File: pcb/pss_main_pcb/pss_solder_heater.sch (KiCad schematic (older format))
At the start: 43 parts, among them J3 Hot Air Gun, J4 Soldering Iron, Q1 BC817, Q2 MMBT2222, Q3 MMBT2907, Q4 IRLML9301T, Q5 IRFZ44S, Q6 BT139B-800, U3 MOC3023S, U4 LM358

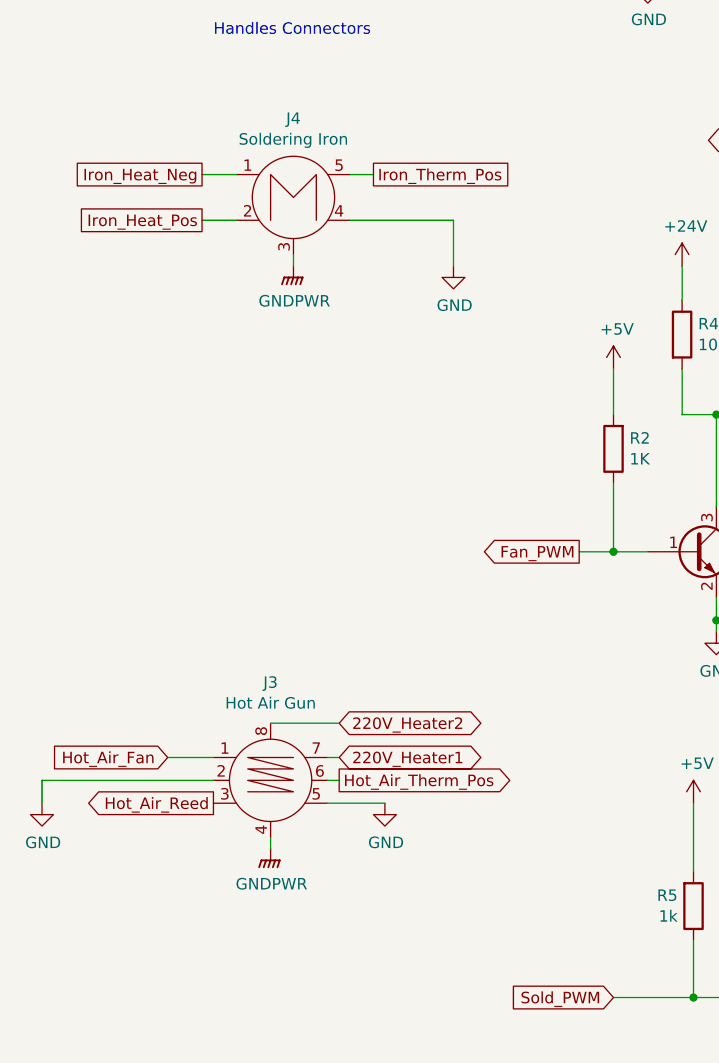
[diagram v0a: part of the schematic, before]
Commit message: Change footprints and place some new components
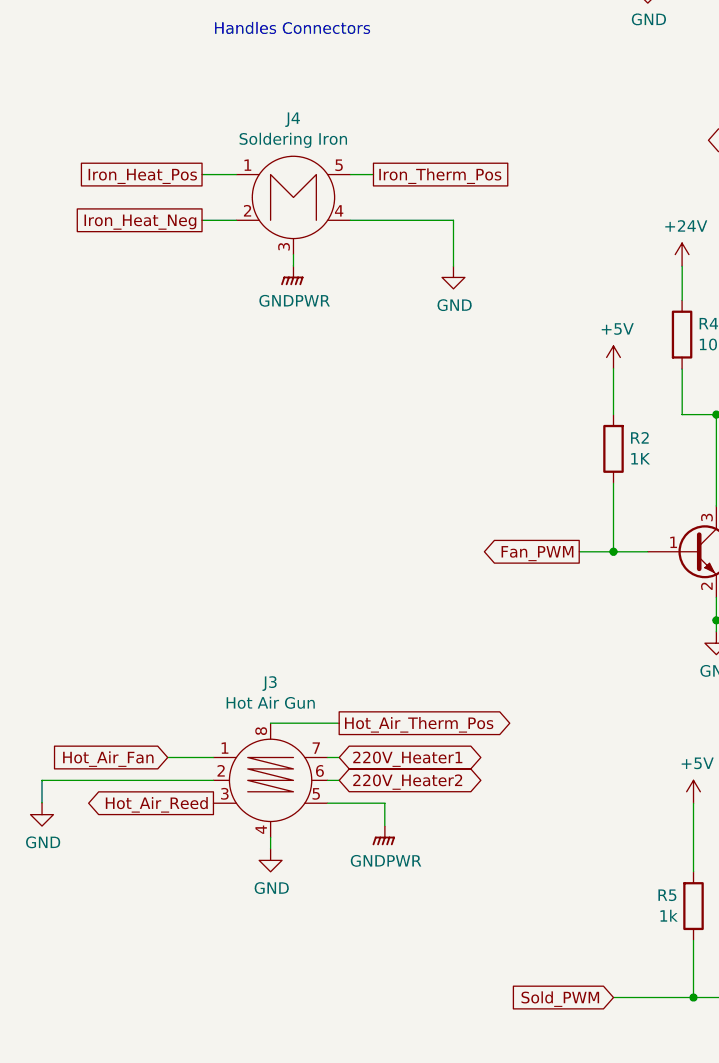
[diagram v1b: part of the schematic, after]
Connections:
- net +24V: now also J4.1; no longer J4.2
- net 220V_Heater2: now also J3.6; no longer J3.8
- net GND: now also J3.4; no longer J3.5
- net GNDPWR: now also J3.5; no longer J3.4
- net Hot_Air_Therm_Pos: now also J3.8; no longer J3.6
- net Iron_Heat_Neg: now also J4.2; no longer J4.1
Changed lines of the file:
@@
 L power:GNDPWR #PWR?
 U 1 1 5EB844F4
-P 1750 5700
+P 2250 5600
 AR Path="/5EB844F4" Ref="#PWR?"  Part="1"
 AR Path="/5EE027BC/5EB844F4" Ref="#PWR?"  Part="1"
 AR Path="/5EE1CBE0/5EB844F4" Ref="#PWR013"  Part="1"
-F 0 "#PWR013" H 1750 5500 50  0001 C CNN
-F 1 "GNDPWR" H 1754 5546 50  0000 C CNN
-F 2 "" H 1750 5650 50  0001 C CNN
-F 3 "" H 1750 5650 50  0001 C CNN
-	1    1750 5700
+F 0 "#PWR013" H 2250 5400 50  0001 C CNN
+F 1 "GNDPWR" H 2254 5446 50  0000 C CNN
+F 2 "" H 2250 5550 50  0001 C CNN
+F 3 "" H 2250 5550 50  0001 C CNN
+	1    2250 5600
 	1    0    0    -1
 $EndComp
 Wire Wire Line
 	1750 5700 1750 5650
-Text GLabel 1450 2950 0    50   UnSpc ~ 0
+Text GLabel 1450 2750 0    50   UnSpc ~ 0
 Iron_Heat_Pos
 Wire Wire Line
 	1450 2750 1600 2750
-Text GLabel 1450 2750 0    50   UnSpc ~ 0
+Text GLabel 1450 2950 0    50   UnSpc ~ 0
 Iron_Heat_Neg
 Wire Wire Line
@@
 L power:GND #PWR?
 U 1 1 5EB8450A
-P 2250 5500
+P 1750 5700
 AR Path="/5EB8450A" Ref="#PWR?"  Part="1"
 AR Path="/5EE027BC/5EB8450A" Ref="#PWR?"  Part="1"
 AR Path="/5EE1CBE0/5EB8450A" Ref="#PWR015"  Part="1"
-F 0 "#PWR015" H 2250 5250 50  0001 C CNN
-F 1 "GND" H 2255 5327 50  0000 C CNN
-F 2 "" H 2250 5500 50  0001 C CNN
-F 3 "" H 2250 5500 50  0001 C CNN
-	1    2250 5500
+F 0 "#PWR015" H 1750 5450 50  0001 C CNN
+F 1 "GND" H 1755 5527 50  0000 C CNN
+F 2 "" H 1750 5700 50  0001 C CNN
+F 3 "" H 1750 5700 50  0001 C CNN
+	1    1750 5700
 	1    0    0    -1
 $EndComp
@@
 Wire Wire Line
 	2100 2950 2550 2950
-Text GLabel 2050 5400 2    50   Output ~ 0
+Text GLabel 2050 5150 2    50   Output ~ 0
 Hot_Air_Therm_Pos
 Wire Wire Line
@@
 Wire Wire Line
 	2000 5300 2050 5300
-Text GLabel 2050 5150 2    50   BiDi ~ 0
+Text GLabel 2050 5400 2    50   BiDi ~ 0
 220V_Heater2
 Text Notes 1500 2150 0    50   ~ 0
@@
 $EndComp
 Connection ~ 5700 6000
+Wire Wire Line
+	2250 5600 2250 5500
 $EndSCHEMATC

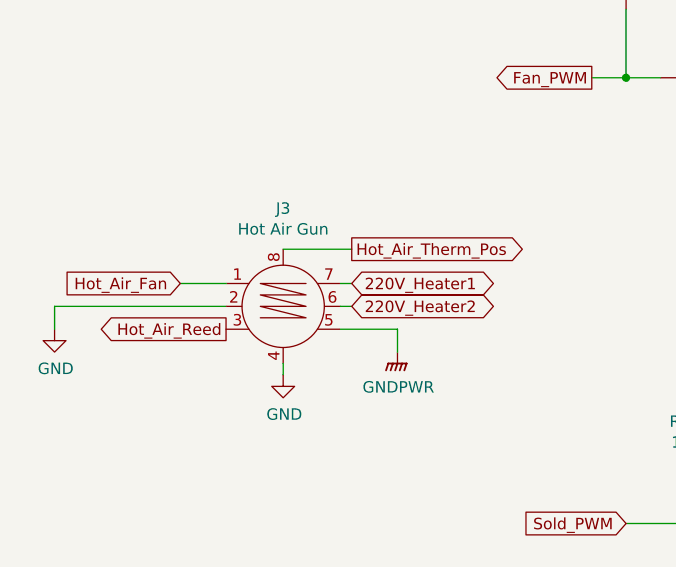
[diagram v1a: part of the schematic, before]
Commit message: Started pcb routing
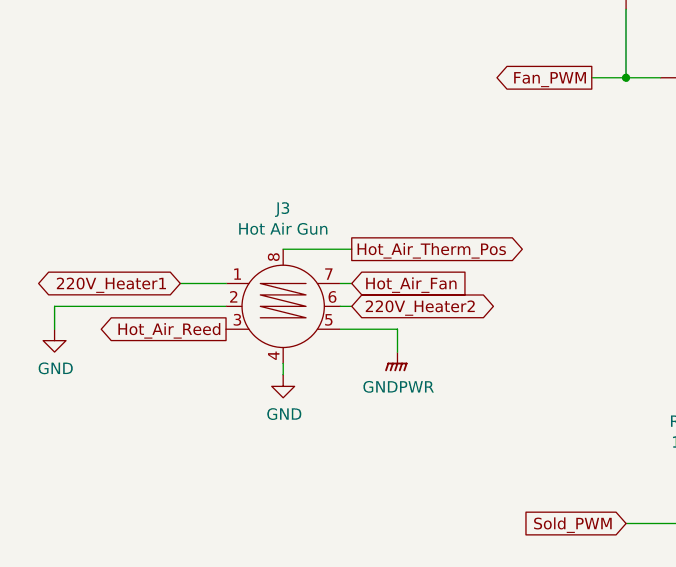
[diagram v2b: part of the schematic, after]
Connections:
- net 220V_Heater1: now also J3.1; no longer J3.7
- net Hot_Air_Fan: now also J3.7; no longer J3.1
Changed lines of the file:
@@
 	1    0    0    -1
 $EndComp
-Text GLabel 1300 5300 0    50   Input ~ 0
+Text GLabel 2050 5300 2    50   Input ~ 0
 Hot_Air_Fan
 Wire Wire Line
@@
 Wire Wire Line
 	2000 5400 2050 5400
-Text GLabel 2050 5300 2    50   BiDi ~ 0
+Text GLabel 1300 5300 0    50   BiDi ~ 0
 220V_Heater1
 Wire Wire Line

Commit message: Change routing
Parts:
- R10: footprint Resistor_SMD:R_1206_3216Metric_Pad1.42x1.75mm_HandSolder -> Resistor_SMD:R_2512_6332Metric_Pad1.52x3.35mm_HandSolder
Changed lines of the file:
@@
 F 0 "R10" H 5270 2096 50  0000 L CNN
 F 1 "51 1W" H 5270 2005 50  0000 L CNN
-F 2 "Resistor_SMD:R_1206_3216Metric_Pad1.42x1.75mm_HandSolder" V 5130 2050 50  0001 C CNN
+F 2 "Resistor_SMD:R_2512_6332Metric_Pad1.52x3.35mm_HandSolder" V 5130 2050 50  0001 C CNN
 F 3 "~" H 5200 2050 50  0001 C CNN
 	1    5200 2050

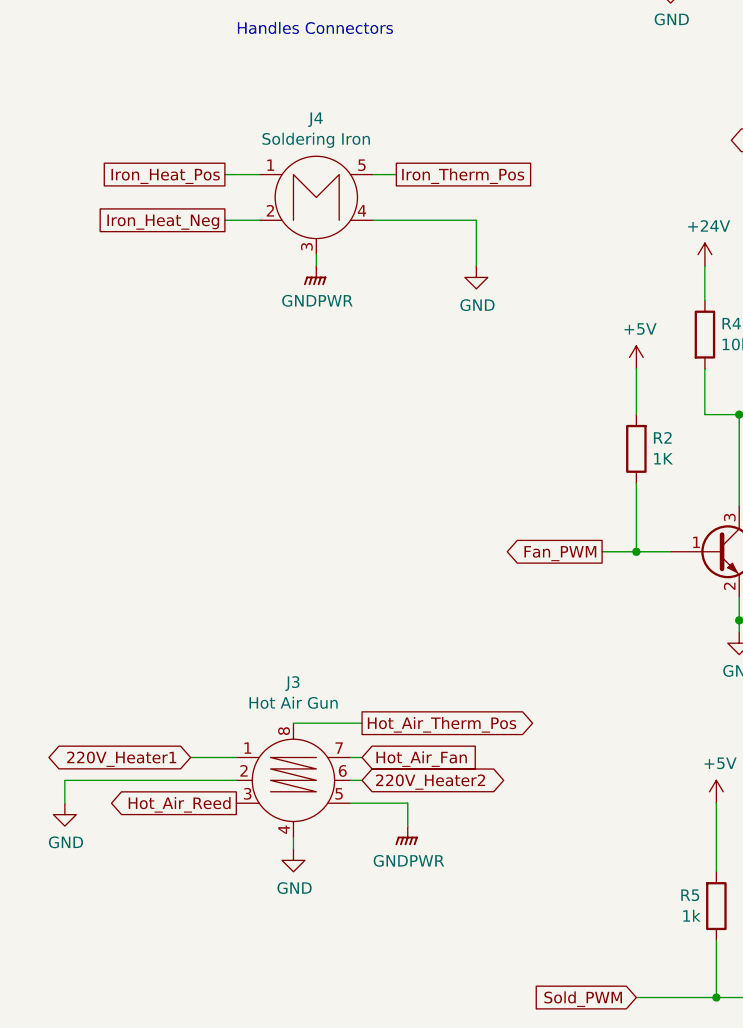
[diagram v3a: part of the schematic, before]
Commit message: Add new routes
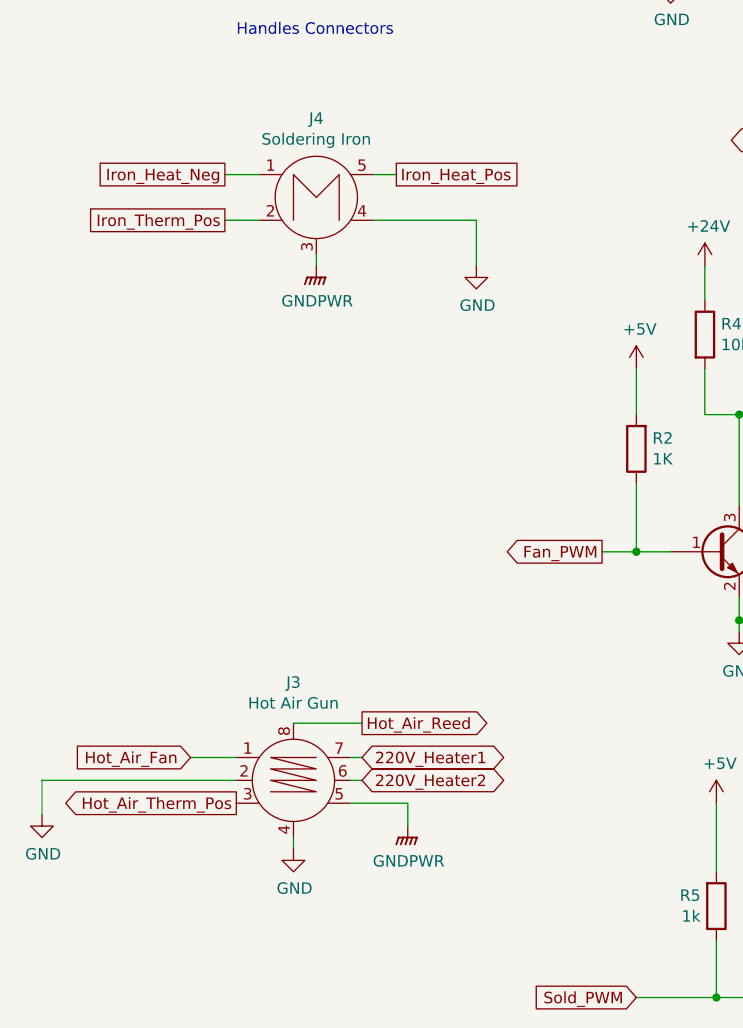
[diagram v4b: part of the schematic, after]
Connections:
- net +24V: now also J4.5; no longer J4.1
- net 220V_Heater1: now also J3.7; no longer J3.1
- net Hot_Air_Fan: now also J3.1; no longer J3.7
- net Hot_Air_Reed: now also J3.8; no longer J3.3
- net Hot_Air_Therm_Pos: now also J3.3; no longer J3.8
- net Iron_Heat_Neg: now also J4.1; no longer J4.2
- net Iron_Therm_Pos: now also J4.2; no longer J4.5
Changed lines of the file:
@@
 Wire Wire Line
 	1750 5700 1750 5650
-Text GLabel 1450 2750 0    50   UnSpc ~ 0
+Text GLabel 2200 2750 2    50   UnSpc ~ 0
 Iron_Heat_Pos
 Wire Wire Line
 	1450 2750 1600 2750
-Text GLabel 1450 2950 0    50   UnSpc ~ 0
+Text GLabel 1450 2750 0    50   UnSpc ~ 0
 Iron_Heat_Neg
 Wire Wire Line
 	1450 2950 1600 2950
-Text GLabel 2200 2750 2    50   UnSpc ~ 0
+Text GLabel 1450 2950 0    50   UnSpc ~ 0
 Iron_Therm_Pos
 Wire Wire Line
@@
 L power:GND #PWR?
 U 1 1 5EB84501
-P 750 5500
+P 650 5550
 AR Path="/5EB84501" Ref="#PWR?"  Part="1"
 AR Path="/5EE027BC/5EB84501" Ref="#PWR?"  Part="1"
 AR Path="/5EE1CBE0/5EB84501" Ref="#PWR012"  Part="1"
-F 0 "#PWR012" H 750 5250 50  0001 C CNN
-F 1 "GND" H 755 5327 50  0000 C CNN
-F 2 "" H 750 5500 50  0001 C CNN
-F 3 "" H 750 5500 50  0001 C CNN
-	1    750  5500
+F 0 "#PWR012" H 650 5300 50  0001 C CNN
+F 1 "GND" H 655 5377 50  0000 C CNN
+F 2 "" H 650 5550 50  0001 C CNN
+F 3 "" H 650 5550 50  0001 C CNN
+	1    650  5550
 	1    0    0    -1
 $EndComp
-Text GLabel 2050 5300 2    50   Input ~ 0
+Text GLabel 1300 5300 0    50   Input ~ 0
 Hot_Air_Fan
 Wire Wire Line
 	1300 5300 1500 5300
-Text GLabel 1500 5500 0    50   Output ~ 0
+Text GLabel 2050 5150 2    50   Output ~ 0
 Hot_Air_Reed
 $Comp
@@
 Wire Wire Line
 	2100 2950 2550 2950
-Text GLabel 2050 5150 2    50   Output ~ 0
+Text GLabel 1500 5500 0    50   Output ~ 0
 Hot_Air_Therm_Pos
 Wire Wire Line
 	2000 5400 2050 5400
-Text GLabel 1300 5300 0    50   BiDi ~ 0
+Text GLabel 2050 5300 2    50   BiDi ~ 0
 220V_Heater1
 Wire Wire Line
@@
 Wire Wire Line
 	2050 5150 1750 5150
-Wire Wire Line
-	750  5500 750  5400
-Wire Wire Line
-	750  5400 1500 5400
 $Comp
 L gx16_conn:GX16-M5_connector J?
@@
 Wire Wire Line
 	2250 5600 2250 5500
+Wire Wire Line
+	650  5550 650  5400
+Wire Wire Line
+	650  5400 1500 5400
 $EndSCHEMATC

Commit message: Add 3D models and totaly redesign PCB
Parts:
- C6: footprint Capacitor_SMD:CP_Elec_8x10.5 -> Capacitor_SMD:CP_Elec_8x10
- C8: footprint Capacitor_SMD:CP_Elec_4x5.4 -> Capacitor_SMD:CP_Elec_4x5.3
- L3: footprint Inductor_SMD:L_Taiyo-Yuden_NR-30xx_HandSoldering -> Inductor_SMD:L_0805_2012Metric_Pad1.15x1.40mm_HandSolder
- Q6: footprint bt139b:D2PAK-3 -> Package_TO_SOT_SMD:TO-263-2
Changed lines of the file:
@@
 F 0 "L3" V 5690 3400 50  0000 C CNN
 F 1 "1u" V 5599 3400 50  0000 C CNN
-F 2 "Inductor_SMD:L_Taiyo-Yuden_NR-30xx_HandSoldering" H 5500 3400 50  0001 C CNN
+F 2 "Inductor_SMD:L_0805_2012Metric_Pad1.15x1.40mm_HandSolder" H 5500 3400 50  0001 C CNN
 F 3 "~" H 5500 3400 50  0001 C CNN
 	1    5500 3400
@@
 F 0 "C6" H 5965 3696 50  0000 L CNN
 F 1 "47u 50V" H 5650 3500 50  0000 L CNN
-F 2 "Capacitor_SMD:CP_Elec_8x10.5" H 5850 3650 50  0001 C CNN
+F 2 "Capacitor_SMD:CP_Elec_8x10" H 5850 3650 50  0001 C CNN
 F 3 "~" H 5850 3650 50  0001 C CNN
 	1    5850 3650
@@
 F 0 "C8" H 8915 5696 50  0000 L CNN
 F 1 "10u 16V" H 8800 5550 50  0000 L CNN
-F 2 "Capacitor_SMD:CP_Elec_4x5.4" H 8800 5650 50  0001 C CNN
+F 2 "Capacitor_SMD:CP_Elec_4x5.3" H 8800 5650 50  0001 C CNN
 F 3 "~" H 8800 5650 50  0001 C CNN
 	1    8800 5650
@@
 F 0 "Q6" H 5829 1746 50  0000 L CNN
 F 1 "BT139B-800" H 5829 1655 50  0000 L CNN
-F 2 "bt139b:D2PAK-3" H 5900 1625 50  0001 L CIN
+F 2 "Package_TO_SOT_SMD:TO-263-2" H 5900 1625 50  0001 L CIN
 F 3 "https://www.ariat-tech.com/datasheet/42/SBR545D1-13.pdf" H 5700 1700 50  0001 L CNN
 	1    5700 1700
